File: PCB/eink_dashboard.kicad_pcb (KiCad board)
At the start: 2 copper layers, 64.5 x 55.4 mm, 60 parts, among them J1 USB_B_Micro, J2 Conn_01x05, Q1 IRLML6402, Q2 IRLML6402, Q3 IRLML6402, Q4 IRLML6402, U1 LM358, U10 CD4094, U11 CD4094, U2 MCP73831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

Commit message: Mitsudomoe symbol and board title added on silkscreen
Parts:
- added G***: LOGO, Custom:Mitsudomoe, F.Cu at (173.7, 86.4)
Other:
- board text added: "E-Ink Dashboard Michał Lisak 2019"

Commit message: R6 changed to 2k
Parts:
- R6: value TBD -> 2k
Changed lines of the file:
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@@
   (page A4)
   (layers
-    (0 F.Cu signal hide)
-    (31 B.Cu signal hide)
+    (0 F.Cu signal)
+    (31 B.Cu signal)
     (32 B.Adhes user)
     (33 F.Adhes user)
@@
       (effects (font (size 1 1) (thickness 0.15)))
     )
-    (fp_text value TBD (at 0 1.75 90) (layer F.Fab)
-      (effects (font (size 1 1) (thickness 0.15)))
-    )
+    (fp_text value 2k (at 0 1.75 90) (layer F.Fab)
+      (effects (font (size 1 1) (thickness 0.15)))
+    )

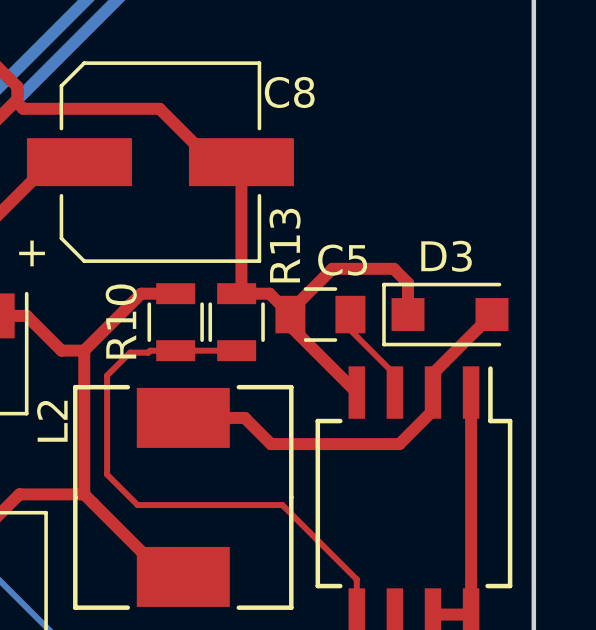
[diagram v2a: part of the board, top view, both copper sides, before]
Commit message: IMPORTANT FIX: D3 direction switched
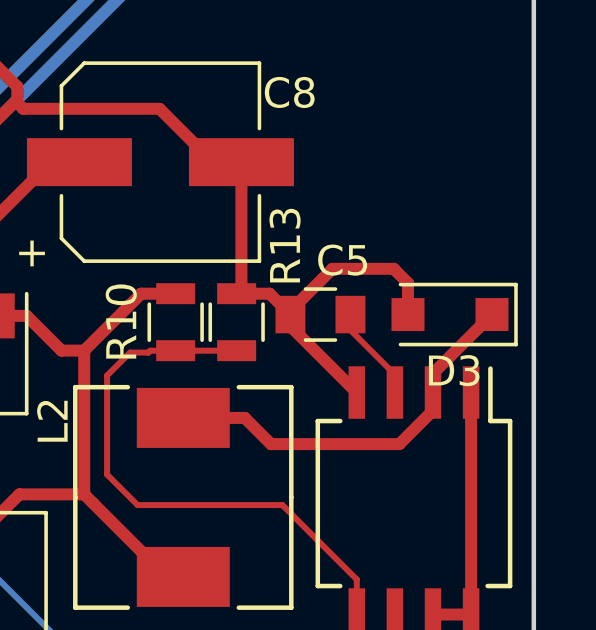
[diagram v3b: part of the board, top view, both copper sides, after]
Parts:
- turned D3 to 180 degrees
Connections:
- D3 pad 1: -20V -> Net-(D3-Pad1)
- D3 pad 2: Net-(D3-Pad2) -> -20V
- L2 pad 1: Net-(D3-Pad2) -> Net-(D3-Pad1)
- U4 pad 2: Net-(D3-Pad2) -> Net-(D3-Pad1)
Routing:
- net Net-(D3-Pad2): track 13.2 -> 0.00 mm
- net Net-(D3-Pad1): track 0.00 -> 13.2 mm

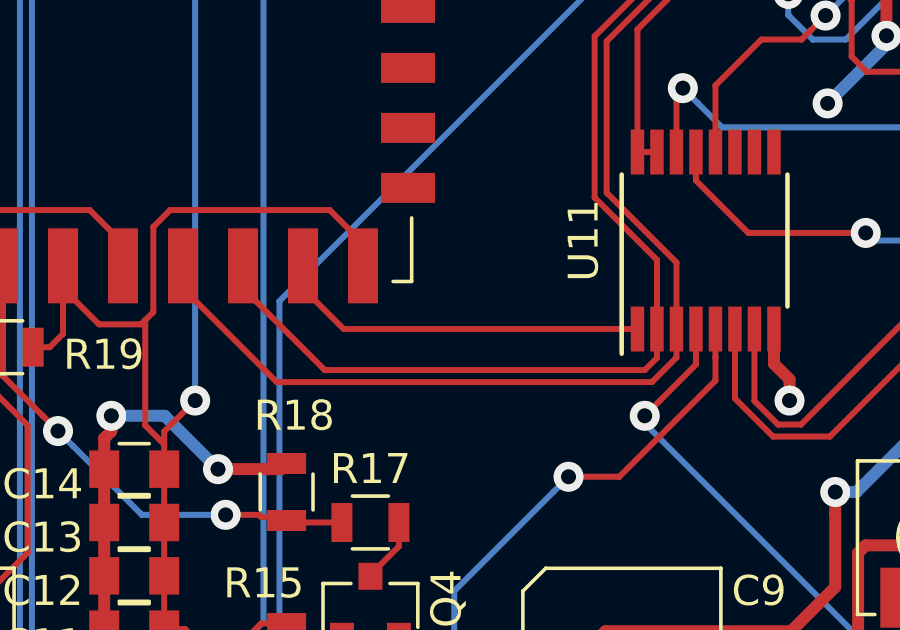
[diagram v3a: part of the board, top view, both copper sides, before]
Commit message: IMPORTANT FIX: D and STR swapped on ESP module
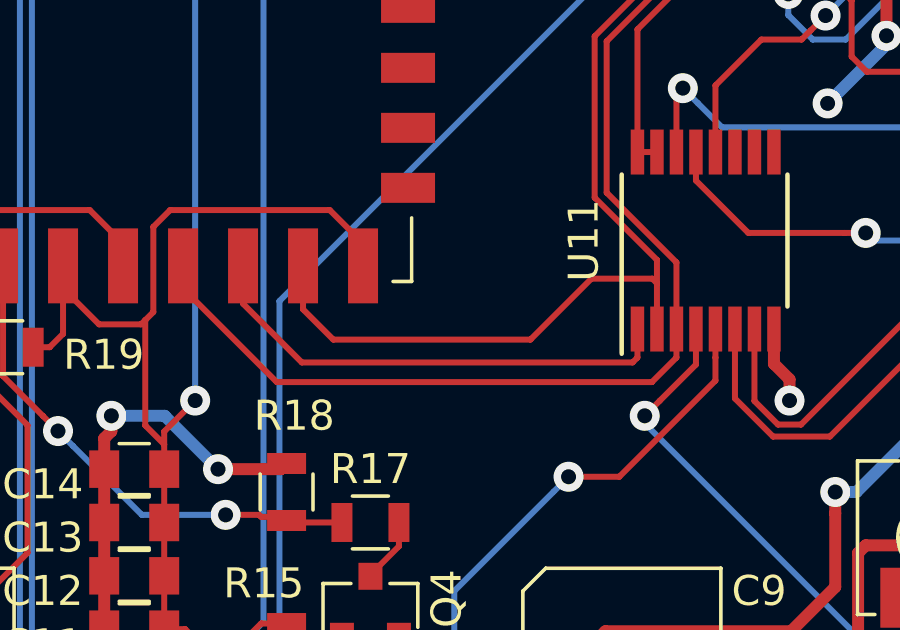
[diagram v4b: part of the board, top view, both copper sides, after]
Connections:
- U9 pad 6: D -> STR
- U9 pad 7: STR -> D
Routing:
- net STR: track 12.5 -> 16.2 mm
- net D: track 32.0 -> 29.8 mm
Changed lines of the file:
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@@
     (thickness 1.6)
     (drawings 7)
-    (tracks 810)
+    (tracks 814)
     (zones 0)
     (modules 61)
@@
       (net 10 +3V3))
     (pad 7 smd rect (at -7.6 8.5 90) (size 2.5 1) (layers F.Cu F.Paste F.Mask)
-      (net 65 STR))
-    (pad 6 smd rect (at -7.6 6.5 90) (size 2.5 1) (layers F.Cu F.Paste F.Mask)
       (net 64 D))
+    (pad 6 smd rect (at -7.6 6.5 90) (size 2.5 1) (layers F.Cu F.Paste F.Mask)
+      (net 65 STR))
     (pad 5 smd rect (at -7.6 4.5 90) (size 2.5 1) (layers F.Cu F.Paste F.Mask)
       (net 66 CLK))
@@
   (segment (start 142.028 110.126) (end 143.30701 111.40501) (width 0.4) (layer F.Cu) (net 15))
   (segment (start 141.478 110.126) (end 142.028 110.126) (width 0.5) (layer F.Cu) (net 15))
-  (segment (start 180.281 108.647) (end 180.281 109.28) (width 0.5) (layer F.Cu) (net 72))
-  (segment (start 182.248 106.68) (end 180.281 108.647) (width 0.4) (layer F.Cu) (net 72))
-  (segment (start 180.281 109.88) (end 180.281 109.28) (width 0.5) (layer F.Cu) (net 72))
-  (segment (start 179.163 110.998) (end 180.281 109.88) (width 0.4) (layer F.Cu) (net 72))
-  (segment (start 174.88 110.998) (end 179.163 110.998) (width 0.4) (layer F.Cu) (net 72))
-  (segment (start 171.958 110.126) (end 174.008 110.126) (width 0.4) (layer F.Cu) (net 72))
-  (segment (start 174.008 110.126) (end 174.88 110.998) (width 0.4) (layer F.Cu) (net 72))
   (via (at 122.428 70.104) (size 1) (drill 0.5) (layers F.Cu B.Cu) (net 19))
   (segment (start 122.374 70.158) (end 122.428 70.104) (width 0.2) (layer F.Cu) (net 19))
@@
   (segment (start 148.205998 93.510002) (end 147.421 92.725004) (width 0.2) (layer F.Cu) (net 56))
   (segment (start 156.718 85.766004) (end 148.974002 93.510002) (width 0.2) (layer F.Cu) (net 56))
-  (segment (start 130.374 88.97) (end 130.374 88.22) (width 0.2) (layer F.Cu) (net 64))
-  (segment (start 133.098 91.694) (end 130.374 88.97) (width 0.2) (layer F.Cu) (net 64))
-  (segment (start 143.764 91.694) (end 133.098 91.694) (width 0.2) (layer F.Cu) (net 64))
-  (segment (start 144.171 91.287) (end 143.764 91.694) (width 0.2) (layer F.Cu) (net 64))
-  (segment (start 144.171 90.326) (end 144.171 91.287) (width 0.2) (layer F.Cu) (net 64))
   (segment (start 144.171 78.491002) (end 144.171 77.814) (width 0.2) (layer F.Cu) (net 64))
   (segment (start 142.093989 80.568013) (end 144.171 78.491002) (width 0.2) (layer F.Cu) (net 64))
@@
   (segment (start 142.093989 85.944689) (end 142.093989 80.568013) (width 0.2) (layer F.Cu) (net 64))
   (segment (start 144.171 88.0217) (end 142.093989 85.944689) (width 0.2) (layer F.Cu) (net 64))
-  (segment (start 144.171 90.326) (end 144.171 88.0217) (width 0.2) (layer F.Cu) (net 64))
-  (segment (start 133.73 90.326) (end 143.521 90.326) (width 0.2) (layer F.Cu) (net 65))
-  (segment (start 132.374 88.22) (end 132.374 88.97) (width 0.2) (layer F.Cu) (net 65))
-  (segment (start 132.374 88.97) (end 133.73 90.326) (width 0.2) (layer F.Cu) (net 65))
+  (segment (start 144.018 88.646) (end 144.171 88.799) (width 0.2) (layer F.Cu) (net 64))
+  (segment (start 141.986 88.646) (end 144.018 88.646) (width 0.2) (layer F.Cu) (net 64))
+  (segment (start 144.171 88.799) (end 144.171 88.0217) (width 0.2) (layer F.Cu) (net 64))
+  (segment (start 144.171 90.326) (end 144.171 88.799) (width 0.2) (layer F.Cu) (net 64))
+  (segment (start 132.374 89.67) (end 133.382 90.678) (width 0.2) (layer F.Cu) (net 64))
+  (segment (start 139.954 90.678) (end 141.986 88.646) (width 0.2) (layer F.Cu) (net 64))
+  (segment (start 133.382 90.678) (end 139.954 90.678) (width 0.2) (layer F.Cu) (net 64))
+  (segment (start 132.374 88.22) (end 132.374 89.67) (width 0.2) (layer F.Cu) (net 64))
+  (segment (start 143.521 91.276) (end 143.521 90.326) (width 0.2) (layer F.Cu) (net 65))
+  (segment (start 143.357 91.44) (end 143.521 91.276) (width 0.2) (layer F.Cu) (net 65))
+  (segment (start 132.334 91.44) (end 143.357 91.44) (width 0.2) (layer F.Cu) (net 65))
+  (segment (start 130.374 89.48) (end 132.334 91.44) (width 0.2) (layer F.Cu) (net 65))
+  (segment (start 130.374 88.22) (end 130.374 89.48) (width 0.2) (layer F.Cu) (net 65))
   (segment (start 144.002989 92.094011) (end 131.498011 92.094011) (width 0.2) (layer F.Cu) (net 66))
   (segment (start 131.498011 92.094011) (end 128.374 88.97) (width 0.2) (layer F.Cu) (net 66))
@@
   (segment (start 142.494 80.733702) (end 144.821 78.406702) (width 0.2) (layer F.Cu) (net 66))
   (segment (start 144.821 90.326) (end 144.821 88.106) (width 0.2) (layer F.Cu) (net 66))
+  (segment (start 180.281 108.647) (end 180.281 109.28) (width 0.5) (layer F.Cu) (net 72))
+  (segment (start 182.248 106.68) (end 180.281 108.647) (width 0.4) (layer F.Cu) (net 72))
+  (segment (start 180.281 109.88) (end 180.281 109.28) (width 0.5) (layer F.Cu) (net 72))
+  (segment (start 179.163 110.998) (end 180.281 109.88) (width 0.4) (layer F.Cu) (net 72))
+  (segment (start 174.88 110.998) (end 179.163 110.998) (width 0.4) (layer F.Cu) (net 72))
+  (segment (start 171.958 110.126) (end 174.008 110.126) (width 0.4) (layer F.Cu) (net 72))
+  (segment (start 174.008 110.126) (end 174.88 110.998) (width 0.4) (layer F.Cu) (net 72))
   (zone (net 1) (net_name GND) (layer F.Cu) (hatch edge 0.508)
     (connect_pads (clearance 0.3))

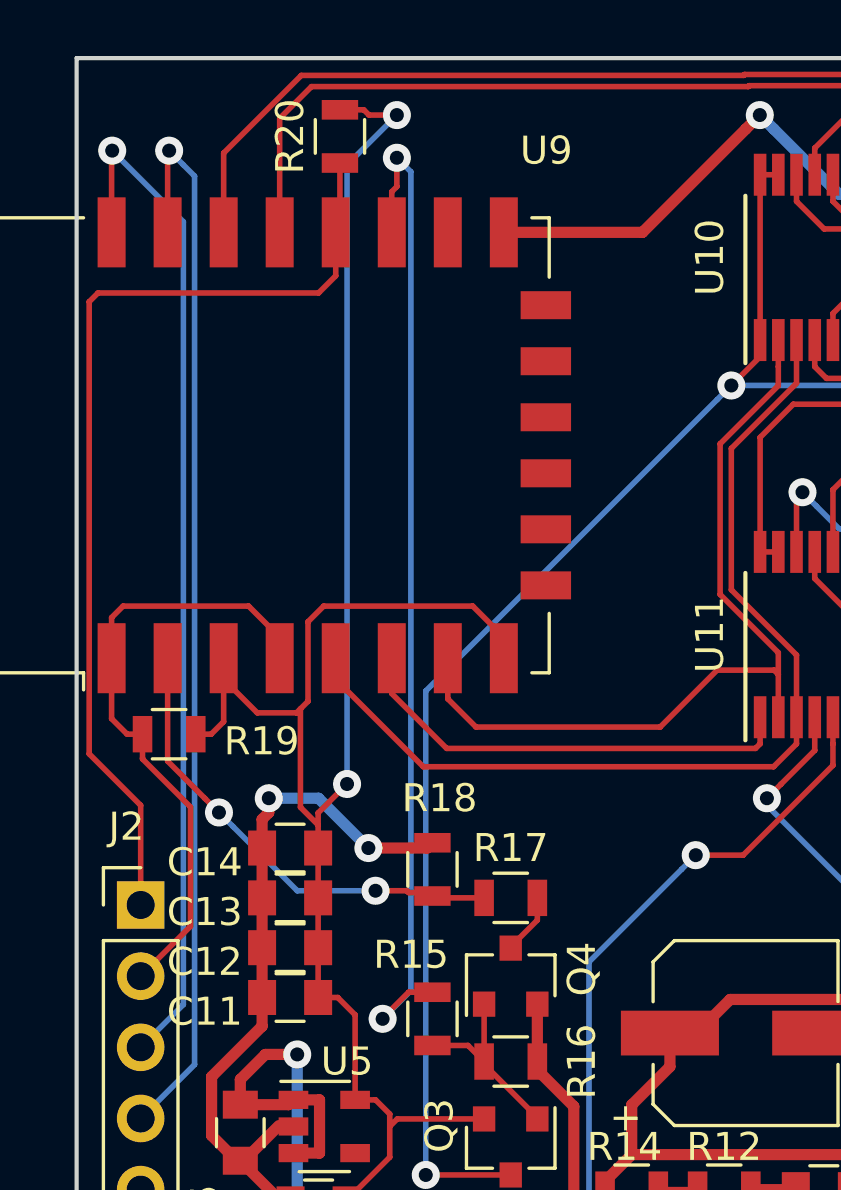
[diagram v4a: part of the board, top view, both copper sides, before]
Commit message: Changed EINK_EN to GPIO15 (was GPIO2)
This is to not interfere with LED present on ESP12 modules
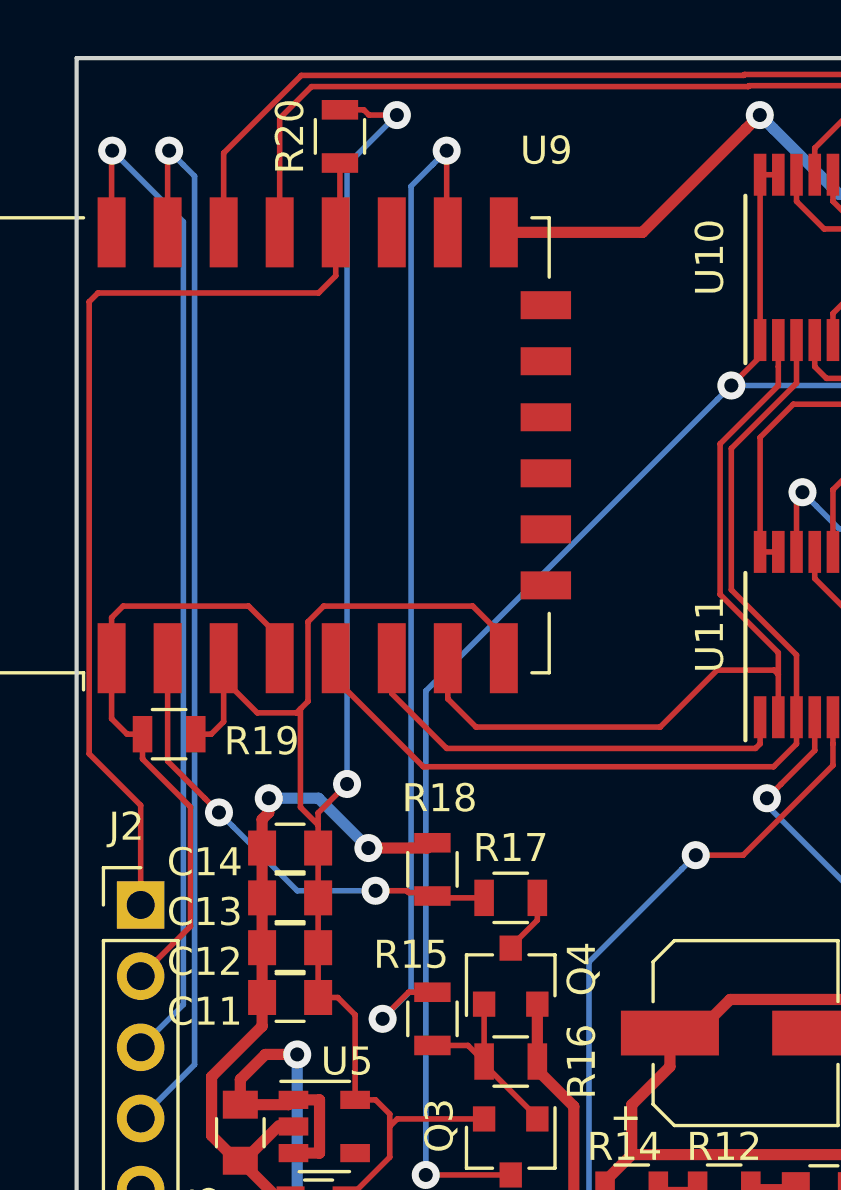
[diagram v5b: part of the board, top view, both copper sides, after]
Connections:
- U9 pad 16: Net-(U9-Pad16) -> EINK_EN
- U9 pad 17: EINK_EN -> Net-(U9-Pad17)
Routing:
- net EINK_EN: track 36.3 -> 37.1 mm
